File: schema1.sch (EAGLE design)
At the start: 35 parts, among them IC1 PIC16F1938SP, IC2 EXCALIBUR, IC3 LP2950CZ, X3 PG203J

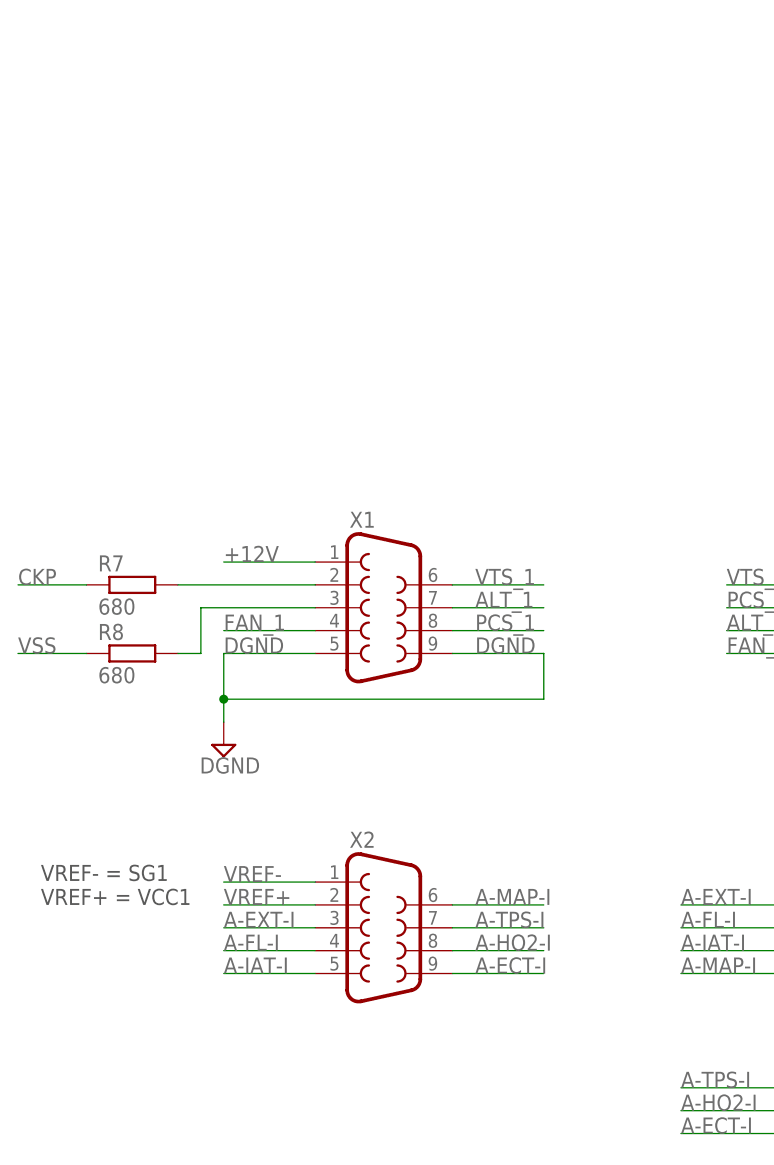
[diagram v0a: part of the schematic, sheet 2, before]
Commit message: Schematic with d-sub25 connector and board pcd file
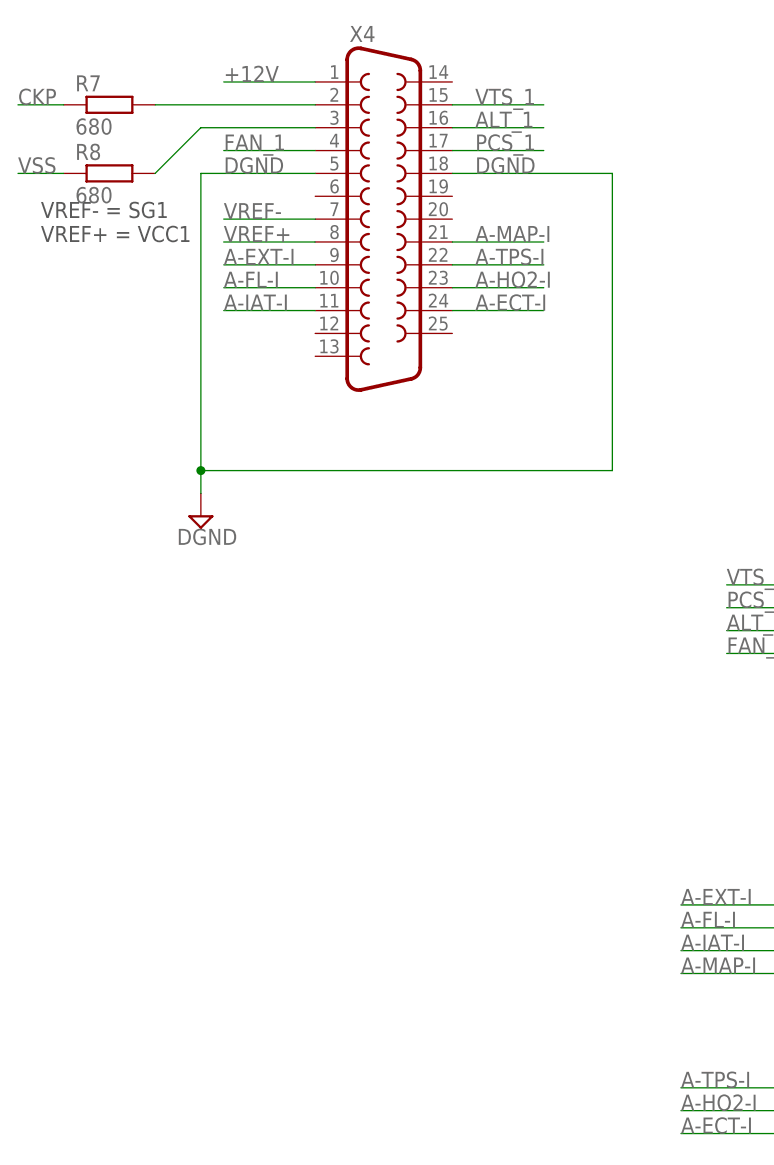
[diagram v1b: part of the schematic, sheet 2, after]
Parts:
- removed X1, X2: (no value), con-subd:F09H
- added X4: (no value), con-subd:F25H
- IC5: value LTC6906 -> (none)
- renumbered U$1 to IC5
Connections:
- net +12V: now also X4.1; no longer X1.1
- net A-ECT-I: now also X4.24; no longer X2.9
- net A-EXT-I: now also X4.9; no longer X2.3
- net A-FL-I: now also X4.10; no longer X2.4
- net A-HO2-I: now also X4.23; no longer X2.8
- net A-IAT-I: now also X4.11; no longer X2.5
- net A-MAP-I: now also X4.21; no longer X2.6
- net A-TPS-I: now also X4.22; no longer X2.7
- net ALT_1: now also X4.16; no longer X1.7
- net DGND: now also X4.18, X4.5; no longer X1.5, X1.9
- net FAN_1: now also X4.4; no longer X1.4
- net N$11: now also X4.3; no longer X1.3
- net N$9: now also X4.2; no longer X1.2
- net PCS_1: now also X4.17; no longer X1.8
- net VREF+: now also X4.8; no longer X2.2
- net VREF-: now also X4.7; no longer X2.1
- net VTS_1: now also X4.15; no longer X1.6
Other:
- moved on the sheet: R7, R8

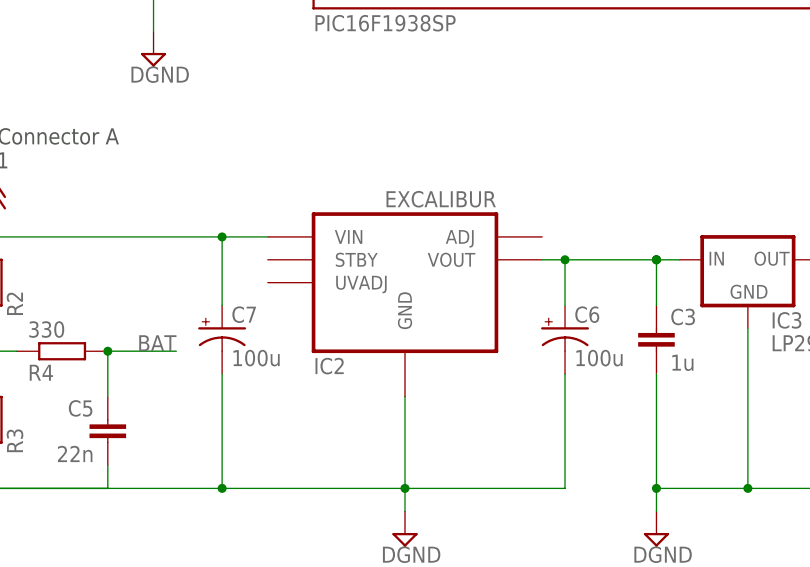
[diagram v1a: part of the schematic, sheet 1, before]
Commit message: Updated excalibur footprint. Updated board.
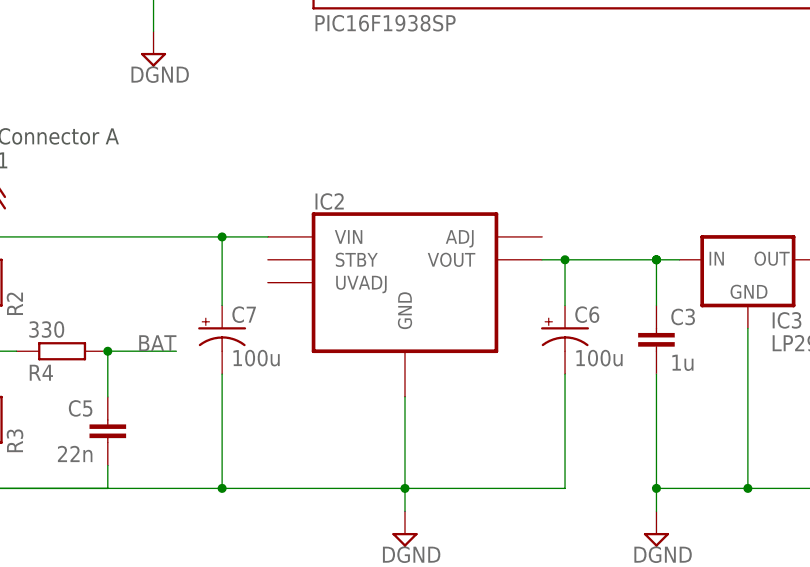
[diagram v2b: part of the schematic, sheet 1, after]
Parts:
- IC2: value EXCALIBUR -> (none); device julio:EXCALIBUR -> julio:EXCALIBURPKG1360
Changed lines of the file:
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@@
 <grid distance="0.1" unitdist="inch" unit="inch" style="lines" multiple="1" display="no" altdistance="0.01" altunitdist="inch" altunit="inch"/>
 <layers>
-<layer number="1" name="Top" color="4" fill="1" visible="no" active="no"/>
-<layer number="16" name="Bottom" color="1" fill="1" visible="no" active="no"/>
-<layer number="17" name="Pads" color="2" fill="1" visible="no" active="no"/>
-<layer number="18" name="Vias" color="2" fill="1" visible="no" active="no"/>
-<layer number="19" name="Unrouted" color="6" fill="1" visible="no" active="no"/>
-<layer number="20" name="Dimension" color="15" fill="1" visible="no" active="no"/>
-<layer number="21" name="tPlace" color="7" fill="1" visible="no" active="no"/>
-<layer number="22" name="bPlace" color="7" fill="1" visible="no" active="no"/>
-<layer number="23" name="tOrigins" color="15" fill="1" visible="no" active="no"/>
-<layer number="24" name="bOrigins" color="15" fill="1" visible="no" active="no"/>
-<layer number="25" name="tNames" color="7" fill="1" visible="no" active="no"/>
-<layer number="26" name="bNames" color="7" fill="1" visible="no" active="no"/>
-<layer number="27" name="tValues" color="7" fill="1" visible="no" active="no"/>
-<layer number="28" name="bValues" color="7" fill="1" visible="no" active="no"/>
+<layer number="1" name="Top" color="4" fill="1" visible="yes" active="no"/>
+<layer number="16" name="Bottom" color="1" fill="1" visible="yes" active="no"/>
+<layer number="17" name="Pads" color="2" fill="1" visible="yes" active="no"/>
+<layer number="18" name="Vias" color="2" fill="1" visible="yes" active="no"/>
+<layer number="19" name="Unrouted" color="6" fill="1" visible="yes" active="no"/>
+<layer number="20" name="Dimension" color="15" fill="1" visible="yes" active="no"/>
+<layer number="21" name="tPlace" color="7" fill="1" visible="yes" active="no"/>
+<layer number="22" name="bPlace" color="7" fill="1" visible="yes" active="no"/>
+<layer number="23" name="tOrigins" color="15" fill="1" visible="yes" active="no"/>
+<layer number="24" name="bOrigins" color="15" fill="1" visible="yes" active="no"/>
+<layer number="25" name="tNames" color="7" fill="1" visible="yes" active="no"/>
+<layer number="26" name="bNames" color="7" fill="1" visible="yes" active="no"/>
+<layer number="27" name="tValues" color="7" fill="1" visible="yes" active="no"/>
+<layer number="28" name="bValues" color="7" fill="1" visible="yes" active="no"/>
 <layer number="29" name="tStop" color="7" fill="3" visible="no" active="no"/>
 <layer number="30" name="bStop" color="7" fill="6" visible="no" active="no"/>
@@
 <layer number="35" name="tGlue" color="7" fill="4" visible="no" active="no"/>
 <layer number="36" name="bGlue" color="7" fill="5" visible="no" active="no"/>
-<layer number="37" name="tTest" color="7" fill="1" visible="no" active="no"/>
-<layer number="38" name="bTest" color="7" fill="1" visible="no" active="no"/>
+<layer number="37" name="tTest" color="7" fill="1" visible="yes" active="no"/>
+<layer number="38" name="bTest" color="7" fill="1" visible="yes" active="no"/>
 <layer number="39" name="tKeepout" color="4" fill="11" visible="no" active="no"/>
 <layer number="40" name="bKeepout" color="1" fill="11" visible="no" active="no"/>
@@
 <layer number="44" name="Drills" color="7" fill="1" visible="no" active="no"/>
 <layer number="45" name="Holes" color="7" fill="1" visible="no" active="no"/>
-<layer number="46" name="Milling" color="3" fill="1" visible="no" active="no"/>
-<layer number="47" name="Measures" color="7" fill="1" visible="no" active="no"/>
-<layer number="48" name="Document" color="7" fill="1" visible="no" active="no"/>
-<layer number="49" name="Reference" color="7" fill="1" visible="no" active="no"/>
-<layer number="51" name="tDocu" color="6" fill="1" visible="no" active="no"/>
-<layer number="52" name="bDocu" color="7" fill="1" visible="no" active="no"/>
+<layer number="46" name="Milling" color="3" fill="1" visible="yes" active="no"/>
+<layer number="47" name="Measures" color="7" fill="1" visible="yes" active="no"/>
+<layer number="48" name="Document" color="7" fill="1" visible="yes" active="no"/>
+<layer number="49" name="Reference" color="7" fill="1" visible="yes" active="no"/>
+<layer number="51" name="tDocu" color="7" fill="1" visible="yes" active="no"/>
+<layer number="52" name="bDocu" color="7" fill="1" visible="yes" active="no"/>
 <layer number="90" name="Modules" color="5" fill="1" visible="yes" active="yes"/>
 <layer number="91" name="Nets" color="2" fill="1" visible="yes" active="yes"/>
@@
 <part name="GND14" library="supply2" deviceset="DGND" device=""/>
 <part name="P+6" library="supply1" deviceset="VCC" device=""/>
-<part name="IC2" library="julio" deviceset="EXCALIBUR" device=""/>
+<part name="IC2" library="julio" deviceset="EXCALIBUR" device="PKG1360"/>
 <part name="P+8" library="supply1" deviceset="+12V" device=""/>
 <part name="GND18" library="supply2" deviceset="DGND" device=""/>

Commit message: modified:   julio.lbr 	modified:   schema1.brd 	modified:   schema1.sch
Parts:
- removed C13, C14: 22n, capacitor-wima:C5/3
- removed R22: 27k 1%, resistor:R-EU_M0805
- removed R24: 787 1%, resistor:R-EU_0207/7
- removed R25: 680, resistor:R-EU_M1206
- removed SP1: F/EE17P, buzzer:F/EE17P
- added C10, C9: 22n, capacitor-wima:C5/3
- added R10: 680, resistor:R-EU_M1206
- added R12, R15: (no value), julio:RESISTOR_ARRAY
- added SG1, SG2: (no value), con-lstb:MA04-1
- C1: value (none) -> 22n
- C2: value 22n -> 100u; device capacitor-wima:C5/3 -> resistor:CPOL-USE5-10.5
- C3: value 1u -> 100u; device capacitor-wima:C5/2.5 -> resistor:CPOL-USE5-10.5
- C4: value 2n2 -> 1u
- C5: value 22n -> 2n2; device capacitor-wima:C5/3 -> capacitor-wima:C5/2.5
- C6: value 100u -> (none); device resistor:CPOL-USE5-10.5 -> capacitor-wima:C5/3
- C7: value 100u -> 22n; device resistor:CPOL-USE5-10.5 -> capacitor-wima:C5/3
- IC1: value PIC16F1938SP -> (none); device microchip:PIC16F1938SP -> julio:EXCALIBURPKG1360
- IC2: value (none) -> PIC16F1938SP; device julio:EXCALIBURPKG1360 -> microchip:PIC16F1938SP
- LED1: device led:LED5MM -> led:LEDCHIP-LED0805
- R1: value 270k -> 68k
- R11: value 68k -> (none)
- R14: value 33k -> (none)
- R2: value 68k -> 33k
- R3: value 33k -> 330
- R4: value 330 -> 270k
- R5: value 680 -> 787 1%; device julio:RESISTOR_ARRAY -> resistor:R-EU_M0805; R17 68K -> (none)
- R6: value 680 -> 27k 1%; device julio:RESISTOR_ARRAY -> resistor:R-EU_M0805; R17 68K -> (none)
- X3: value PG203J -> 1503_07; device con-hirschmann:PG203J -> con-lumberg:1503_07
- renumbered C12 to C8, IC5 to IC4, R17 to R11, R18 to R14, SV2 to SV1, X4 to X2
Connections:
- removed net N$10: C3.1, C6.+, IC2.VOUT, IC3.IN
- removed net N$11: R8.2, X2.3
- removed net N$4: IC1.SEG6/SCL/SCK/RC3
- removed net N$5: IC1.RC4/SDI/SDA/T1G/SEG11
- removed net VCC: C4.1, IC1.VDD, IC3.OUT, IC4.DIV, IC4.V+, LED1.A, R1.2, SV1.2
- new net +12VR: C3.+, C4.2, IC1.VOUT, IC3.IN, SG2.1
- new net N$7: R9.1, X2.1
- new net SCL: IC2.SEG6/SCL/SCK/RC3, SG2.3
- new net SDA: IC2.RC4/SDI/SDA/T1G/SEG11, SG2.2
- new net VDD: C5.2, IC2.VDD, IC3.OUT, IC4.DIV, IC4.V+, LED1.A, R4.1, SV1.2
- net !MCLR: now also IC2.VPP/!MCLR!/RE3, R4.2; no longer IC1.VPP/!MCLR!/RE3, R1.1
- net +12V: now also C2.+, IC1.VIN, R1.1, X2.12; no longer C7.+, IC2.VIN, R2.2, X2.1
- net A-ECT-I: now also R15.P$5; no longer R6.P$7
- net A-EXT-I: now also R12.P$1, X2.21; no longer R5.P$1, X2.9
- net A-FL-I: now also R12.P$5, X2.22; no longer R5.P$3, X2.10
- net A-HO2-I: now also R15.P$3, X2.11; no longer R6.P$5, X2.23
- net A-IAT-I: now also R12.P$3, X2.9; no longer R5.P$5, X2.11
- net A-MAP-I: now also R12.P$7, X2.10; no longer R5.P$7, X2.21
- net A-TPS-I: now also R15.P$1, X2.23; no longer R6.P$3, X2.22
- net ALT: now also C9.2, IC2.RC5/SDO/SEG10; no longer C13.1, IC1.RC5/SDO/SEG10
- net ALT_1: now also X2.4; no longer X2.16
- net BAT: now also C1.2, IC2.SEG4/CCP5/SRQ/T0CKI/CPS6/C1OUT/RA4, R3.2; no longer C5.1, IC1.SEG4/CCP5/SRQ/T0CKI/CPS6/C1OUT/RA4, R4.2
- net BEEP: now also IC2.RB3/AN9/C12IN2-/CPS3/CCP2/P2A/VLCD3, R8.2; no longer IC1.RB3/AN9/C12IN2-/CPS3/CCP2/P2A/VLCD3, R9.2
- net CKP: now also IC2.SEG3/P1A/CCP1/RC2, R10.2; no longer IC1.SEG3/P1A/CCP1/RC2, R7.1
- net DGND: now also C1.1, C10.1, C2.-, C3.-, C4.1, C5.1, C6.2, C7.1, C9.1, IC1.GND, IC2.VSS, IC2.VSS@1, R2.1, R5.2, R7.1, SG1.4, SG2.4; no longer C1.2, C13.2, C14.2, C2.2, C3.2, C4.2, C5.2, C6.-, C7.-, IC1.VSS, IC1.VSS@1, IC2.GND, R24.1, R25.1, R3.1, SP1.2
- net ECT: now also IC2.SEG12/VCAP/SS/SRNQ/C2OUT/C12IN0-/AN0/RA0, R15.P$6; no longer IC1.SEG12/VCAP/SS/SRNQ/C2OUT/C12IN0-/AN0/RA0, R6.P$8
- net EXT: now also IC2.RB5/AN13/CPS5/P2B/CCP3/P3A/T1G/COM1, R12.P$2; no longer IC1.RB5/AN13/CPS5/P2B/CCP3/P3A/T1G/COM1, R5.P$2
- net FAN: now also C10.2, IC2.SEG1/VCAP/CLKOUT/OSC2/RA6; no longer C14.1, IC1.SEG1/VCAP/CLKOUT/OSC2/RA6
- net FAN_1: now also X2.17; no longer X2.4
- net FLV: now also C6.1, IC2.RB2/AN8/CPS2/P1B/VLCD2, R12.P$6; no longer C1.1, IC1.RB2/AN8/CPS2/P1B/VLCD2, R5.P$4
- net HO2: now also IC2.SEG7/C12IN1-/AN1/RA1, R15.P$4; no longer IC1.SEG7/C12IN1-/AN1/RA1, R6.P$6
- net IAT: now also IC2.SEG5/VCAP/SS/SRNQ/CPS7/C2OUT/AN4/RA5, R12.P$4; no longer IC1.SEG5/VCAP/SS/SRNQ/CPS7/C2OUT/AN4/RA5, R5.P$6
- net ICSPCLK: now also IC2.RB6/ICSPCLK/ICDCLK/SEG14; no longer IC1.RB6/ICSPCLK/ICDCLK/SEG14
- net ICSPDAT: now also IC2.RB7/ICSPDAT/ICDDAT/SEG13; no longer IC1.RB7/ICSPDAT/ICDDAT/SEG13
- net MAP: now also IC2.RB4/AN11/CPS4/P1D/COM0, R12.P$8; no longer IC1.RB4/AN11/CPS4/P1D/COM0, R5.P$8
- net N$1: now also R8.1, SG1.1; no longer R9.1, SP1.1
- net N$2: now also R6.1; no longer R22.2
- net N$3: now also R7.2; no longer R25.2
- net N$6: now also R5.1, R6.2; no longer R22.1, R24.2
- net N$8: now also R1.2, R2.2, R3.1; no longer R2.1, R3.2, R4.1
- net N$9: now also R10.1, X2.14; no longer R7.2, X2.2
- net PCS: now also IC2.RB1/AN10/C12IN3-/CPS1/P1C/VLCD1; no longer IC1.RB1/AN10/C12IN3-/CPS1/P1C/VLCD1
- net PCS_1: now also X2.16; no longer X2.17
- net T1CKI: now also IC2.P2B/T1CKI/T1OSO/RC0; no longer IC1.P2B/T1CKI/T1OSO/RC0
- net TPS: now also IC2.RB0/AN12/CPS0/CCP4/SRI/INT/SEG0, R15.P$2; no longer IC1.RB0/AN12/CPS0/CCP4/SRI/INT/SEG0, R6.P$4
- net UART_RX: now also IC2.RC7/RX/DT/P3B/SEG8; no longer IC1.RC7/RX/DT/P3B/SEG8
- net UART_TX: now also IC2.RC6/TX/CK/CCP3/P3A/SEG9, X3.3; no longer IC1.RC6/TX/CK/CCP3/P3A/SEG9, X3.5
- net VREF+: now also IC2.SEG15/COM3/VREF+/C1IN+/AN3/RA3, X2.6; no longer IC1.SEG15/COM3/VREF+/C1IN+/AN3/RA3, X2.8
- net VREF-: now also IC2.COM2/DACOUT/VREF-/C2IN+/AN2/RA2; no longer IC1.COM2/DACOUT/VREF-/C2IN+/AN2/RA2
- net VSS: now also IC2.P2A/CCP2/T1OSI/RC1, R9.2; no longer IC1.P2A/CCP2/T1OSI/RC1, R8.1
- net VTS: now also C7.2, IC2.SEG2/CLKIN/OSC1/RA7; no longer C2.1, IC1.SEG2/CLKIN/OSC1/RA7
- net VTS_1: now also X2.3; no longer X2.15
